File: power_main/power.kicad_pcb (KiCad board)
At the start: 4 copper layers, 40.9 x 58 mm, 82 parts, among them IC1 TPS7A2450DBVR, IC2 TPD4S480RUKR, IC3 CAT24C512WI-GT3, J2 DX07P024AJ1R1500, J3 Conn_02x10_Counter_Clockwise, J4 Conn_02x10_Counter_Clockwise, J5 DX07S024JJ2R1300, J6 DX07S024JJ2R1300, Q1 CSD18543Q3A, Q2 2N7002DW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

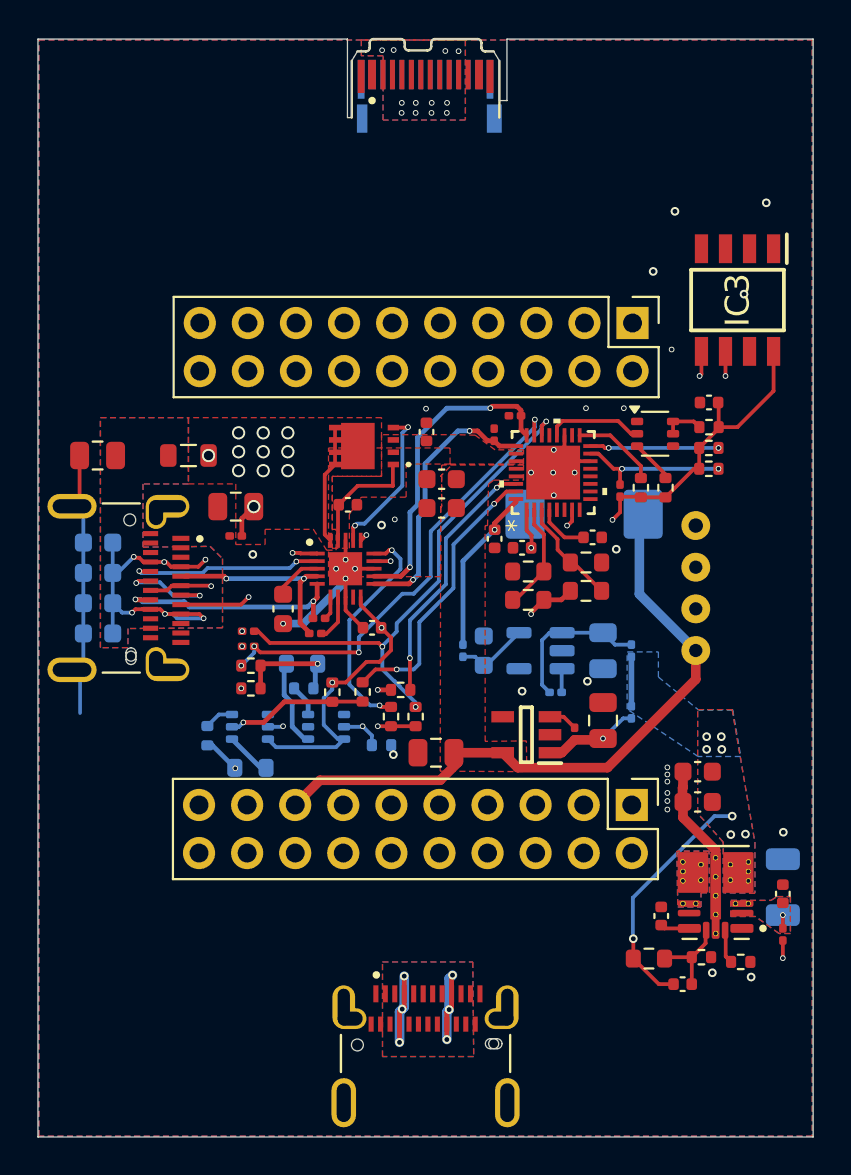
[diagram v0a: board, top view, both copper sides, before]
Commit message: add missing GPIO_PF small trace refactoring
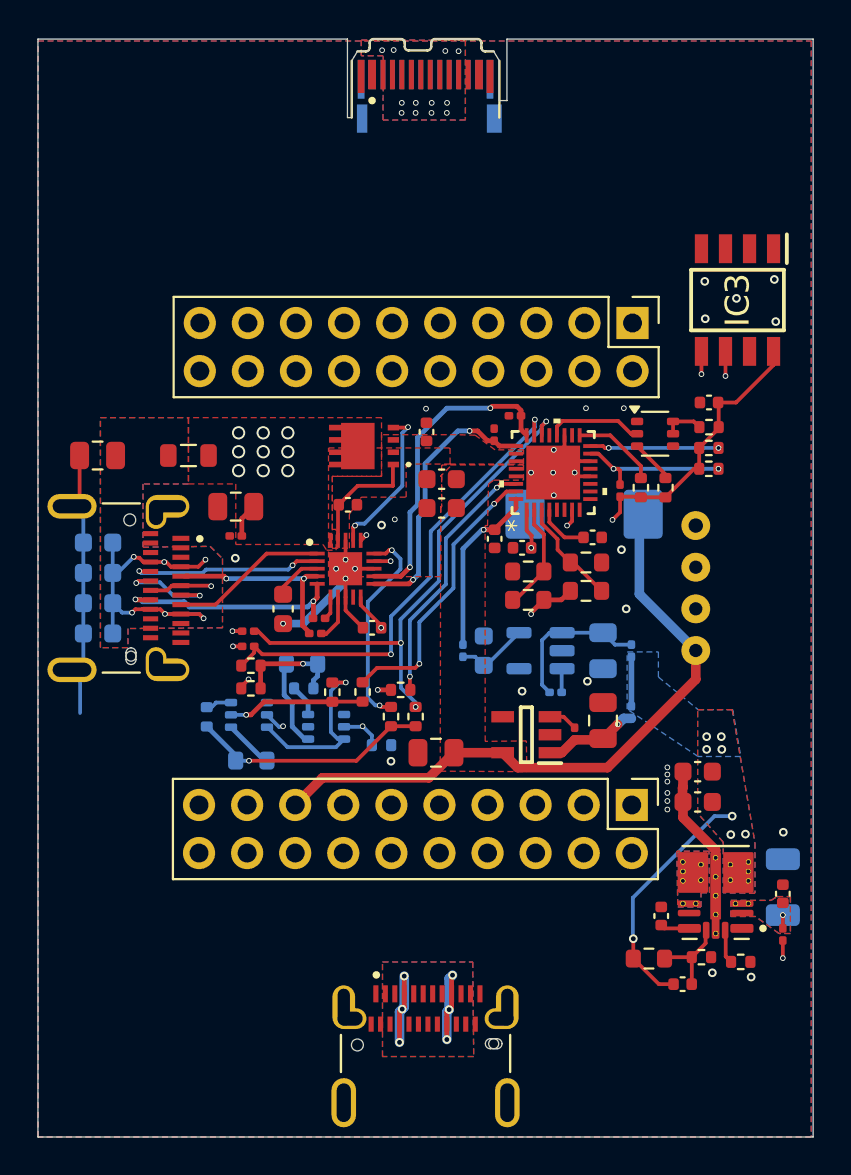
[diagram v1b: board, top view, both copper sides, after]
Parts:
- moved R105 1.00 mm to (119.9, 86.8)
- moved Q9 0.63 mm to (122.2, 86.7)
- moved R101 0.39 mm to (122.3, 89.1)
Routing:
- net +48V: track 23.3 -> 17.0 mm, vias 30 -> 28
- net +3V3: track 54.6 -> 53.0 mm
- net /VIN_3V3: track 8.85 -> 9.82 mm
- net /SBU1: track 12.1 -> 11.1 mm
- net GND: track 31.3 -> 32.2 mm, vias 34 -> 35
- net /GPIO5: track 24.3 -> 25.1 mm, vias 4 -> 2
- net Net-(R101-Pad2): track 12.4 -> 12.7 mm, vias 2 -> 1
- net /C_SBU1: track 8.16 -> 8.32 mm, vias 2 -> 0
